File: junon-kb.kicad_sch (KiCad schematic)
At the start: 4 parts, among them J1 STLINK-V3MINIE, U3 SPX3819M5-L-1-5/TR

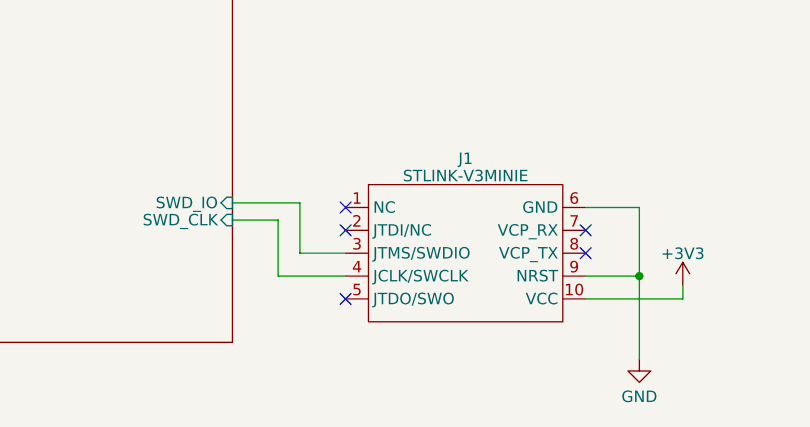
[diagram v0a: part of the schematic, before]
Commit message: update NRST
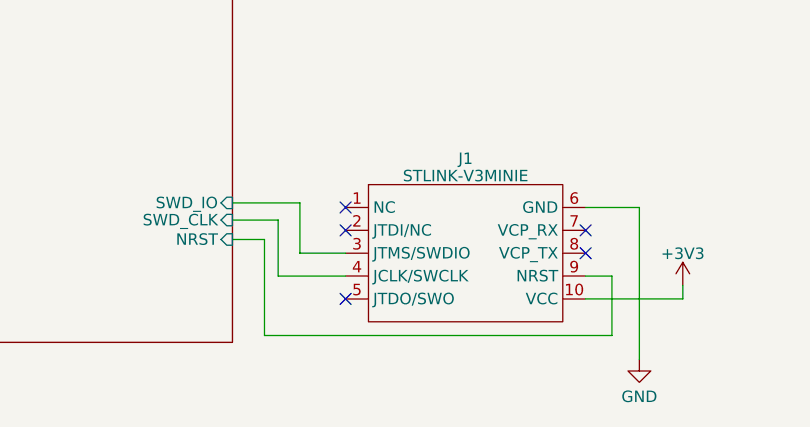
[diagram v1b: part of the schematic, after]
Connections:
- net GND: no longer J1.9 (NRST)
- new net MCU/NRST: J1.9 (NRST)
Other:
- sheet MCU ports: added NRST; removed none
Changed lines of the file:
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@@
 (kicad_sch (version 20230121) (generator eeschema)
   (paper "A4")
-  (junction (at 166.37 124.714) (diameter 0) (color 0 0 0 0)
-  )
   (junction (at 242.697 75.819) (diameter 0) (color 0 0 0 0)
   )
@@
     (stroke (width 0) (type default))
   )
+  (wire (pts (xy 160.401 124.714) (xy 163.322 124.714))
+    (stroke (width 0) (type default))
+  )
   (wire (pts (xy 67.183 79.375) (xy 76.073 79.375))
     (stroke (width 0) (type default))
@@
     (stroke (width 0) (type default))
   )
-  (wire (pts (xy 166.37 124.714) (xy 166.37 133.985))
-    (stroke (width 0) (type default))
-  )
   (wire (pts (xy 67.183 71.755) (xy 76.073 71.755))
     (stroke (width 0) (type default))
   )
+  (wire (pts (xy 124.714 131.318) (xy 163.322 131.318))
+    (stroke (width 0) (type default))
+  )
   (wire (pts (xy 67.183 81.28) (xy 76.073 81.28))
     (stroke (width 0) (type default))
   )
-  (wire (pts (xy 160.401 124.714) (xy 166.37 124.714))
-    (stroke (width 0) (type default))
-  )
   (wire (pts (xy 67.183 109.855) (xy 76.073 109.855))
     (stroke (width 0) (type default))
@@
     (stroke (width 0) (type default))
   )
-  (wire (pts (xy 166.37 117.094) (xy 166.37 124.714))
+  (wire (pts (xy 166.37 117.094) (xy 166.37 133.985))
     (stroke (width 0) (type default))
   )
@@
     (stroke (width 0) (type default))
   )
+  (wire (pts (xy 121.158 120.65) (xy 124.714 120.65))
+    (stroke (width 0) (type default))
+  )
   (wire (pts (xy 240.284 90.551) (xy 242.697 90.551))
     (stroke (width 0) (type default))
@@
   )
   (wire (pts (xy 242.697 75.819) (xy 245.999 75.819))
+    (stroke (width 0) (type default))
+  )
+  (wire (pts (xy 124.714 120.65) (xy 124.714 131.318))
+    (stroke (width 0) (type default))
+  )
+  (wire (pts (xy 163.322 124.714) (xy 163.322 131.318))
     (stroke (width 0) (type default))
   )
@@
       (effects (font (size 1.27 1.27)) (justify left))
     )
-    (instances
+    (pin "NRST" input (at 121.158 120.65 0)
+      (effects (font (size 1.27 1.27)) (justify right))
+    )
+    (instances

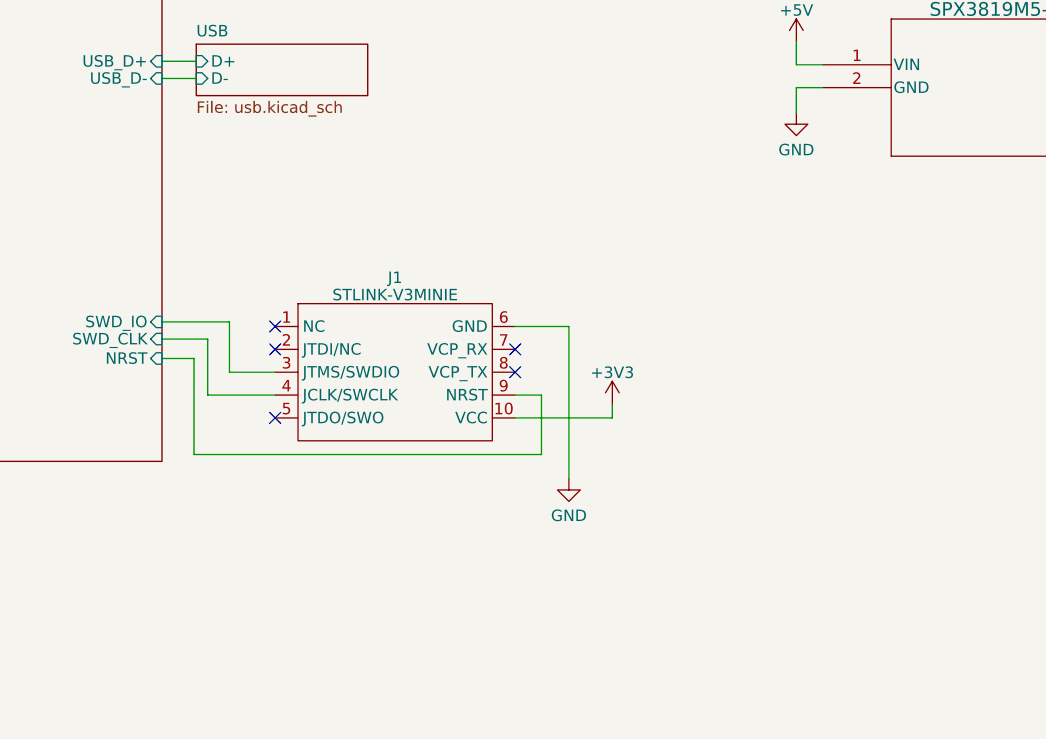
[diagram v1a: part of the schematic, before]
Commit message: flesh out SWD circuit
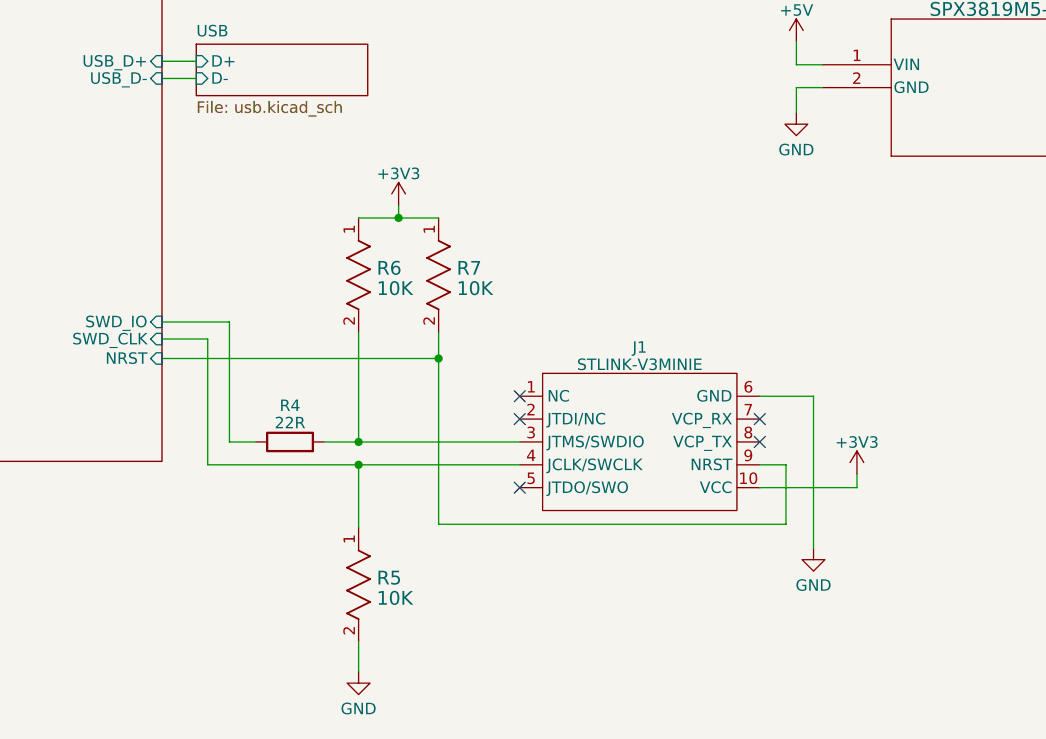
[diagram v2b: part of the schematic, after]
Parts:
- added R4: 22R, Resistor_SMD:R_01005_0402Metric, symbol PCM_Resistor_AKL:R_0402
- added R5, R6, R7: 10K, junon-kb:RES_RK73H1E_KOA, symbol Junon's KB:RK73H1ETTP1002F
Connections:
- net +3V3: now also R6.1, R7.1
- net GND: now also R5.2
- net MCU/NRST: now also R7.2
- net MCU/SWD_CLK: now also R5.1
- net MCU/SWD_IO: now also R4.1; no longer J1.3 (JTMS/SWDIO)
- new net: J1.3 (JTMS/SWDIO), R4.2, R6.2
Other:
- moved on the sheet: J1

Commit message: next version
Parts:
- renumbered C7 to C13, C8 to C14
